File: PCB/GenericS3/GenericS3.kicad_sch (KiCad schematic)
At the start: 64 parts, among them J1 USB-C, J2 Shelly, J5 POWER, P1 33, P10 42, P11 45, P12 46, P13 47, P14 48, P15 18, P16 19, P17 14, P18 15, P19 16, P2 34, P20 17, P21 6, P22 7, P23 8, P24 9, P25 20, P26 10, P27 11, P28 12, P29 13, P3 35, P30 1, P31 2, P32 3, P33 4, P34 5, P35 21, P36 43, P37 44, P38 0, P39 ⏚, P4 36, P40 ⏚, P41 ⏚, P42 ⏚, P5 37, P6 38, P7 39, P8 40, P9 41, U2 ESP32-S3-MINI-1, U5 MD8942

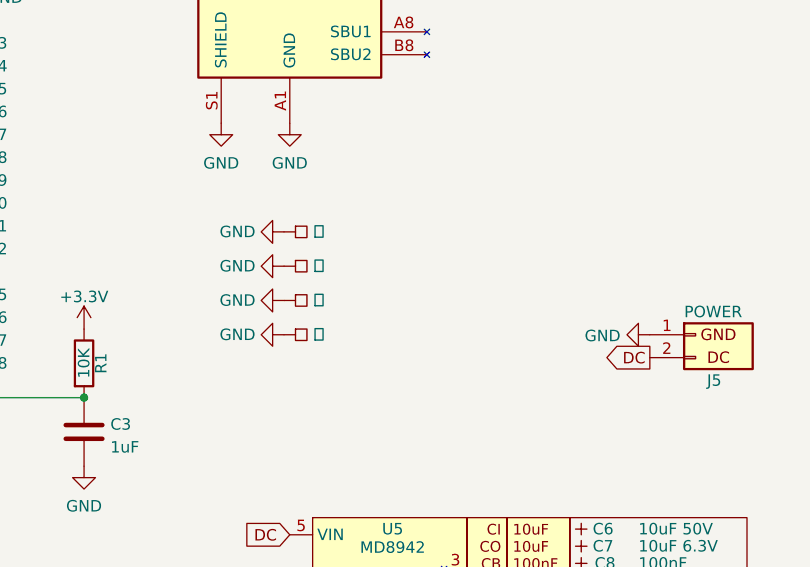
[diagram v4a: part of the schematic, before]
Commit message: Added 3V3 pads as well
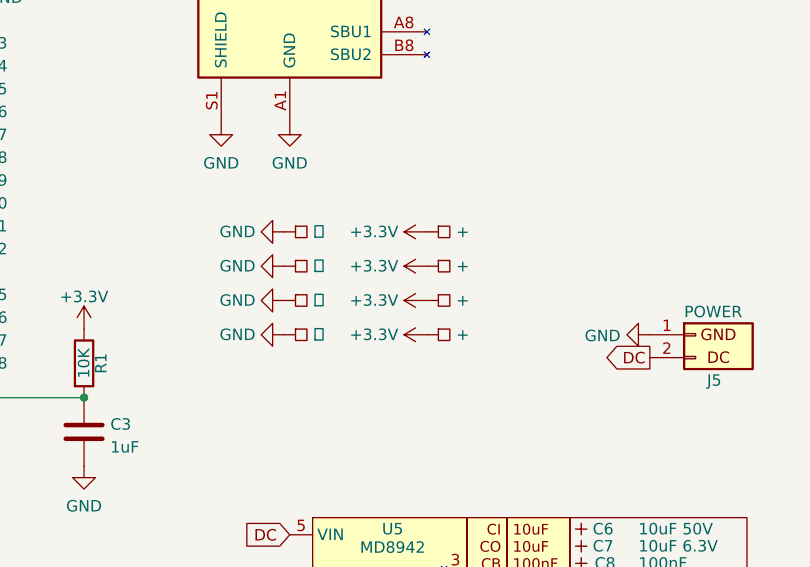
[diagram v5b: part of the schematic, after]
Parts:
- added P43, P44, P45, P46: +, RevK:Square, symbol RevK:Square
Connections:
- net +3.3V: now also P43.1 (P), P44.1 (P), P45.1 (P), P46.1 (P)
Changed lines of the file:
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@@
+    )
+  )
+  (symbol (lib_id "RevK:Square") (at 176.53 100.33 0) (unit 1)
+    (in_bom no) (on_board yes) (dnp no) (fields_autoplaced)
+    (property "Reference" "P46" (at 182.88 100.33 0)
+      (effects (font (size 1.27 1.27)) hide)
+    )
+    (property "Value" "+" (at 179.7812 100.33 0)
+      (effects (font (size 1.27 1.27)) (justify left))
+    )
+    (property "Footprint" "RevK:Square" (at 176.53 102.87 0)
+      (effects (font (size 1.27 1.27)) hide)
+    )
+    (property "Datasheet" "" (at 176.53 100.33 0)
+      (effects (font (size 1.27 1.27)) hide)
+    )
+    (pin "1")
+    (instances
+      (project "GenericS3"
+        (path "/2d210a96-f81f-42a9-8bf4-1b43c11086f3"
+          (reference "P46") (unit 1)
+        )
+      )
     )
   )
@@
     )
   )
+  (symbol (lib_id "RevK:Square") (at 176.53 96.52 0) (unit 1)
+    (in_bom no) (on_board yes) (dnp no) (fields_autoplaced)
+    (property "Reference" "P45" (at 182.88 96.52 0)
+      (effects (font (size 1.27 1.27)) hide)
+    )
+    (property "Value" "+" (at 179.7812 96.52 0)
+      (effects (font (size 1.27 1.27)) (justify left))
+    )
+    (property "Footprint" "RevK:Square" (at 176.53 99.06 0)
+      (effects (font (size 1.27 1.27)) hide)
+    )
+    (property "Datasheet" "" (at 176.53 96.52 0)
+      (effects (font (size 1.27 1.27)) hide)
+    )
+    (pin "1")
+    (instances
+      (project "GenericS3"
+        (path "/2d210a96-f81f-42a9-8bf4-1b43c11086f3"
+          (reference "P45") (unit 1)
+        )
+      )
+    )
+  )
   (symbol (lib_id "RevK:Round") (at 93.98 83.185 180) (unit 1)
     (in_bom no) (on_board yes) (dnp no)
@@
     )
   )
+  (symbol (lib_id "RevK:Square") (at 176.53 92.71 0) (unit 1)
+    (in_bom no) (on_board yes) (dnp no) (fields_autoplaced)
+    (property "Reference" "P44" (at 182.88 92.71 0)
+      (effects (font (size 1.27 1.27)) hide)
+    )
+    (property "Value" "+" (at 179.7812 92.71 0)
+      (effects (font (size 1.27 1.27)) (justify left))
+    )
+    (property "Footprint" "RevK:Square" (at 176.53 95.25 0)
+      (effects (font (size 1.27 1.27)) hide)
+    )
+    (property "Datasheet" "" (at 176.53 92.71 0)
+      (effects (font (size 1.27 1.27)) hide)
+    )
+    (pin "1")
+    (instances
+      (project "GenericS3"
+        (path "/2d210a96-f81f-42a9-8bf4-1b43c11086f3"
+          (reference "P44") (unit 1)
+        )
+      )
+    )
+  )
   (symbol (lib_id "RevK:Round") (at 93.98 57.785 180) (unit 1)
     (in_bom no) (on_board yes) (dnp no)
@@
     )
   )
+  (symbol (lib_id "RevK:Square") (at 176.53 88.9 0) (unit 1)
+    (in_bom no) (on_board yes) (dnp no) (fields_autoplaced)
+    (property "Reference" "P43" (at 182.88 88.9 0)
+      (effects (font (size 1.27 1.27)) hide)
+    )
+    (property "Value" "+" (at 179.7812 88.9 0)
+      (effects (font (size 1.27 1.27)) (justify left))
+    )
+    (property "Footprint" "RevK:Square" (at 176.53 91.44 0)
+      (effects (font (size 1.27 1.27)) hide)
+    )
+    (property "Datasheet" "" (at 176.53 88.9 0)
+      (effects (font (size 1.27 1.27)) hide)
+    )
+    (pin "1")
+    (instances
+      (project "GenericS3"
+        (path "/2d210a96-f81f-42a9-8bf4-1b43c11086f3"
+          (reference "P43") (unit 1)
+        )
+      )
+    )
+  )
+  (symbol (lib_id "power:+3.3V") (at 176.53 96.52 90) (unit 1)
+    (in_bom yes) (on_board yes) (dnp no) (fields_autoplaced)
+    (property "Reference" "#PWR020" (at 180.34 96.52 0)
+      (effects (font (size 1.27 1.27)) hide)
+    )
+    (property "Value" "+3.3V" (at 173.355 96.52 90)
+      (effects (font (size 1.27 1.27)) (justify left))
+    )
+    (property "Footprint" "" (at 176.53 96.52 0)
+      (effects (font (size 1.27 1.27)) hide)
+    )
+    (property "Datasheet" "" (at 176.53 96.52 0)
+      (effects (font (size 1.27 1.27)) hide)
+    )
+    (pin "1")
+    (instances
+      (project "GenericS3"
+        (path "/2d210a96-f81f-42a9-8bf4-1b43c11086f3"
+          (reference "#PWR020") (unit 1)
+        )
+      )
+      (project "Reference"
+        (path "/825c70b0-4860-42b7-97dc-86bfa46e06fd"
+          (reference "#PWR02") (unit 1)
+        )
+      )
+      (project "Generic"
+        (path "/babeabf2-f3b0-4ed5-8d9e-0215947e6cf3"
+          (reference "#PWR024") (unit 1)
+        )
+      )
+    )
+  )
   (symbol (lib_id "RevK:PCB") (at 250.19 172.72 0) (unit 1)
     (in_bom no) (on_board yes) (dnp no)
@@
         (path "/2d210a96-f81f-42a9-8bf4-1b43c11086f3"
           (reference "#PWR08") (unit 1)
+        )
+      )
+    )
+  )
+  (symbol (lib_id "power:+3.3V") (at 176.53 100.33 90) (unit 1)
+    (in_bom yes) (on_board yes) (dnp no) (fields_autoplaced)
+    (property "Reference" "#PWR021" (at 180.34 100.33 0)
+      (effects (font (size 1.27 1.27)) hide)
+    )
+    (property "Value" "+3.3V" (at 173.355 100.33 90)
+      (effects (font (size 1.27 1.27)) (justify left))
+    )
+    (property "Footprint" "" (at 176.53 100.33 0)
+      (effects (font (size 1.27 1.27)) hide)
+    )
+    (property "Datasheet" "" (at 176.53 100.33 0)
+      (effects (font (size 1.27 1.27)) hide)
+    )
+    (pin "1")
+    (instances
+      (project "GenericS3"
+        (path "/2d210a96-f81f-42a9-8bf4-1b43c11086f3"
+          (reference "#PWR021") (unit 1)
+        )
+      )
+      (project "Reference"
+        (path "/825c70b0-4860-42b7-97dc-86bfa46e06fd"
+          (reference "#PWR02") (unit 1)
+        )
+      )
+      (project "Generic"
+        (path "/babeabf2-f3b0-4ed5-8d9e-0215947e6cf3"
+          (reference "#PWR024") (unit 1)
         )
       )
@@
     )
   )
+  (symbol (lib_id "power:+3.3V") (at 176.53 88.9 90) (unit 1)
+    (in_bom yes) (on_board yes) (dnp no) (fields_autoplaced)
+    (property "Reference" "#PWR018" (at 180.34 88.9 0)
+      (effects (font (size 1.27 1.27)) hide)
+    )
+    (property "Value" "+3.3V" (at 173.355 88.9 90)
+      (effects (font (size 1.27 1.27)) (justify left))
+    )
+    (property "Footprint" "" (at 176.53 88.9 0)
+      (effects (font (size 1.27 1.27)) hide)
+    )
+    (property "Datasheet" "" (at 176.53 88.9 0)
+      (effects (font (size 1.27 1.27)) hide)
+    )
+    (pin "1")
+    (instances
+      (project "GenericS3"
+        (path "/2d210a96-f81f-42a9-8bf4-1b43c11086f3"
+          (reference "#PWR018") (unit 1)
+        )
+      )
+      (project "Reference"
+        (path "/825c70b0-4860-42b7-97dc-86bfa46e06fd"
+          (reference "#PWR02") (unit 1)
+        )
+      )
+      (project "Generic"
+        (path "/babeabf2-f3b0-4ed5-8d9e-0215947e6cf3"
+          (reference "#PWR024") (unit 1)
+        )
+      )
+    )
+  )
   (symbol (lib_id "Device:R") (at 138.43 103.505 0) (unit 1)
     (in_bom yes) (on_board yes) (dnp no)
@@
         )
       )
+    )
+  )
+  (symbol (lib_id "power:+3.3V") (at 176.53 92.71 90) (unit 1)
+    (in_bom yes) (on_board yes) (dnp no) (fields_autoplaced)
+    (property "Reference" "#PWR019" (at 180.34 92.71 0)
+      (effects (font (size 1.27 1.27)) hide)
+    )
+    (property "Value" "+3.3V" (at 173.355 92.71 90)
+      (effects (font (size 1.27 1.27)) (justify left))
+    )
+    (property "Footprint" "" (at 176.53 92.71 0)
+      (effects (font (size 1.27 1.27)) hide)
+    )
+    (property "Datasheet" "" (at 176.53 92.71 0)
+      (effects (font (size 1.27 1.27)) hide)
+    )
+    (pin "1")
+    (instances
+      (project "GenericS3"
+        (path "/2d210a96-f81f-42a9-8bf4-1b43c11086f3"
+          (reference "#PWR019") (unit 1)
+        )
+      )
+      (project "Reference"
+        (path "/825c70b0-4860-42b7-97dc-86bfa46e06fd"
+          (reference "#PWR02") (unit 1)
+        )
+      )
+      (project "Generic"
+        (path "/babeabf2-f3b0-4ed5-8d9e-0215947e6cf3"
+          (reference "#PWR024") (unit 1)
+        )
+      )

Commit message: Changed diode
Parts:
- D8: footprint RevK:D_1206 -> RevK:D_SMA; LCSC Part # C143805 -> C8678
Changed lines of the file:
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@@
       (effects (font (size 1.27 1.27)))
     )
-    (property "Footprint" "RevK:D_1206" (at 180.34 38.735 0)
+    (property "Footprint" "RevK:D_SMA" (at 180.34 38.735 0)
       (effects (font (size 1.27 1.27)) hide)
     )
@@
       (effects (font (size 1.27 1.27)) hide)
     )
-    (property "LCSC Part #" "C143805" (at 180.34 38.735 0)
+    (property "LCSC Part #" "C8678" (at 180.34 38.735 0)
       (effects (font (size 1.27 1.27)) hide)
     )

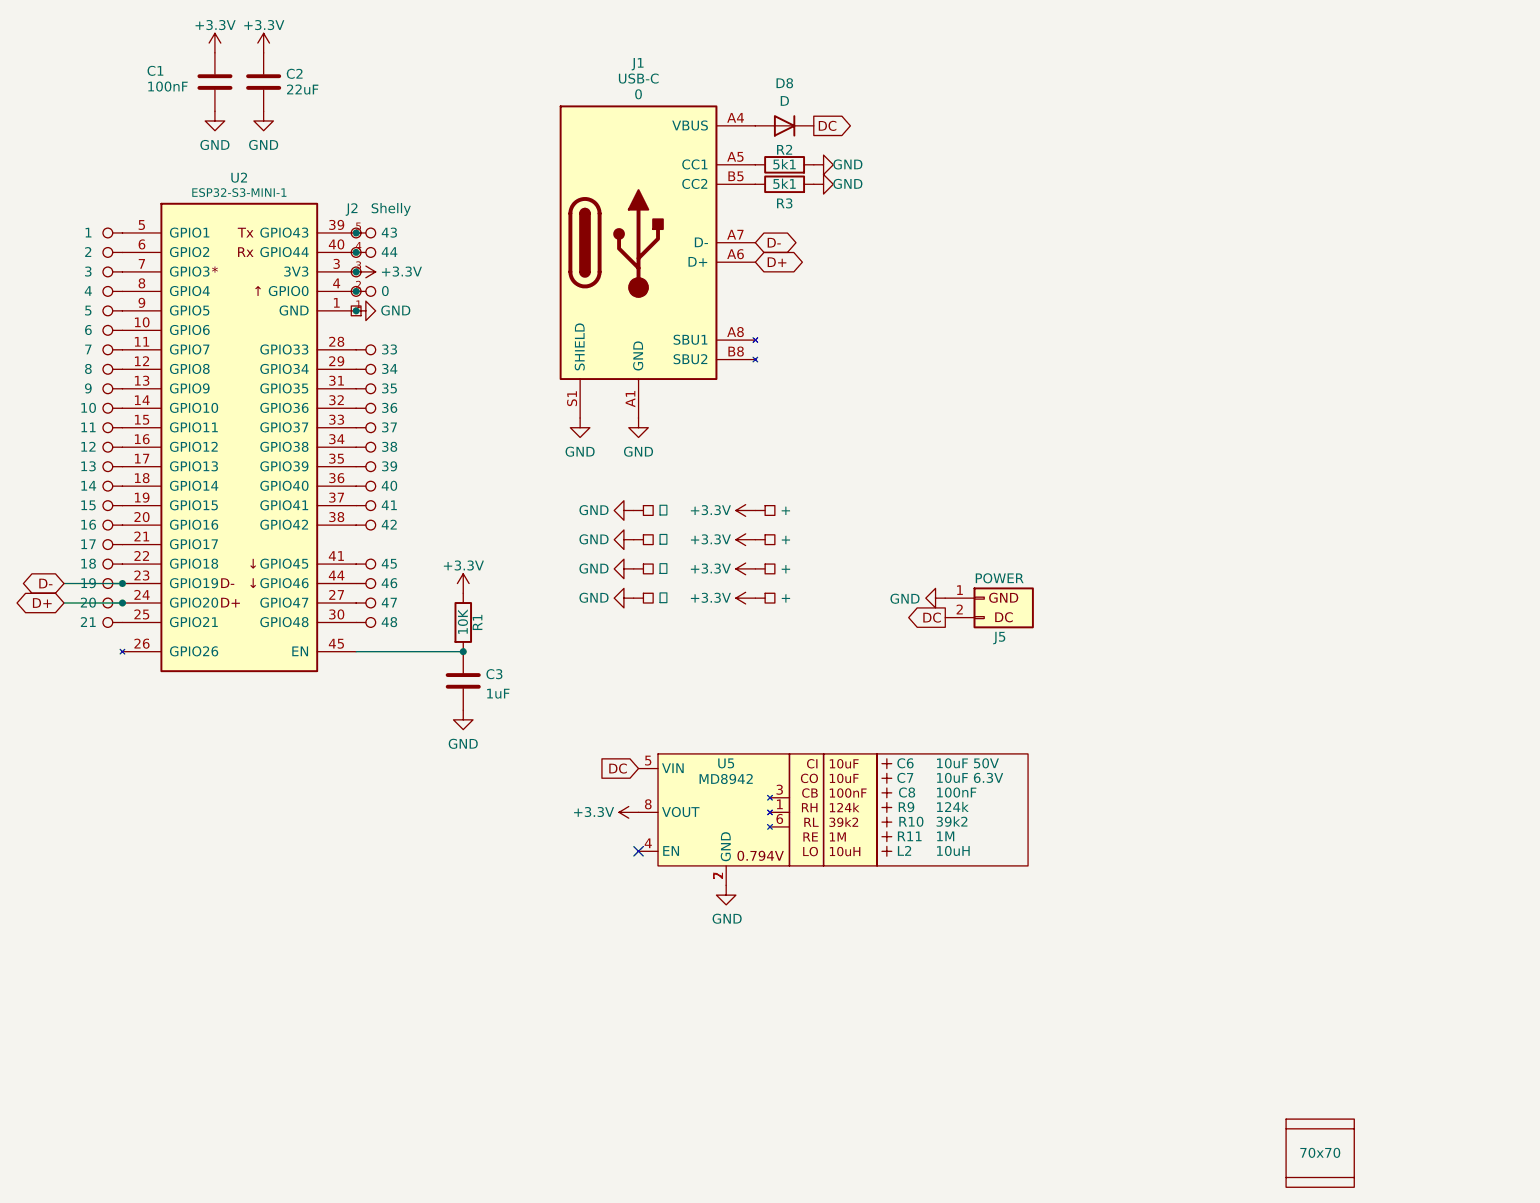
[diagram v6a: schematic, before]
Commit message: Fix diode and barcode
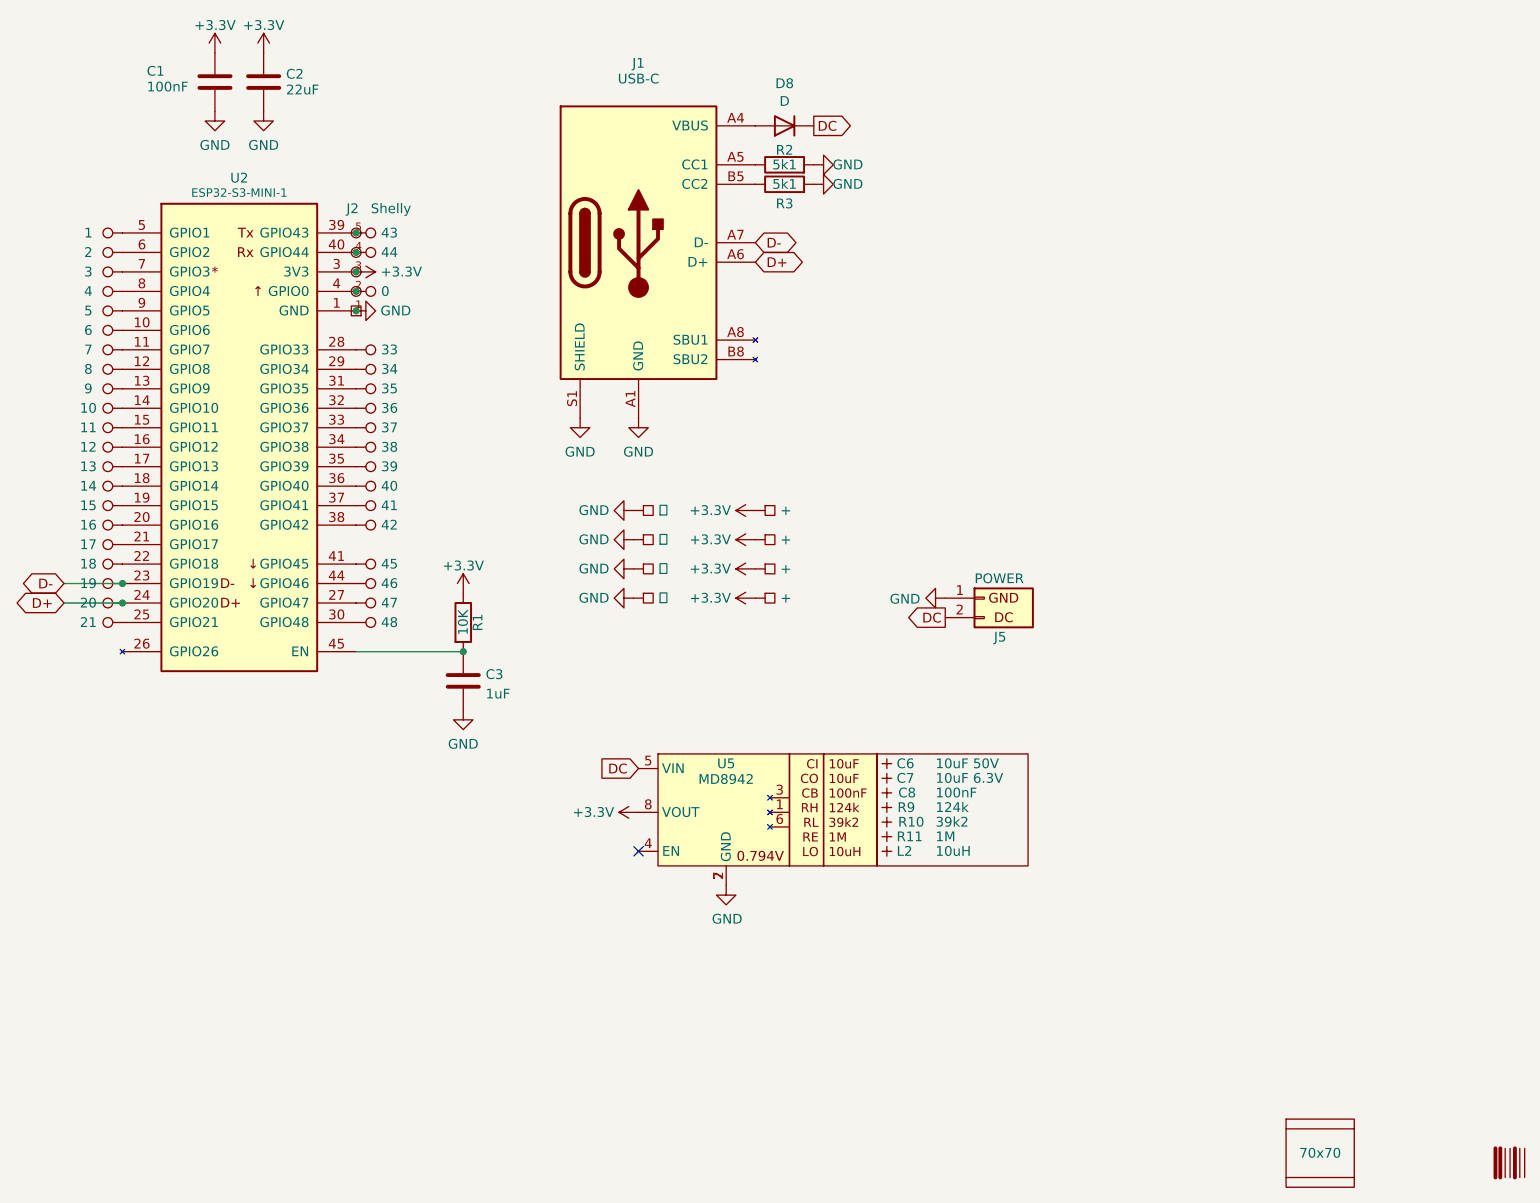
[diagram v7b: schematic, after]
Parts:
- added U1: Barcode, RevK:EAN-5060634238120, symbol RevK:Barcode
- J1: JLCPCB Rotation Offset 0 -> (none)
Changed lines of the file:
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@@
+    )
+  )
+  (symbol (lib_id "RevK:Barcode") (at 274.955 173.99 0) (unit 1)
+    (in_bom no) (on_board yes) (dnp no) (fields_autoplaced)
+    (property "Reference" "U1" (at 274.955 177.165 0)
+      (effects (font (size 1.27 1.27)) hide)
+    )
+    (property "Value" "Barcode" (at 274.955 179.07 0)
+      (effects (font (size 1.27 1.27)) hide)
+    )
+    (property "Footprint" "RevK:EAN-5060634238120" (at 274.32 174.625 0)
+      (effects (font (size 1.27 1.27)) hide)
+    )
+    (property "Datasheet" "" (at 274.32 174.625 0)
+      (effects (font (size 1.27 1.27)) hide)
+    )
+    (property "Note" "Non part, PCB printed" (at 274.955 168.275 0)
+      (effects (font (size 1.27 1.27)) hide)
+    )
+    (instances
+      (project "GenericS3"
+        (path "/2d210a96-f81f-42a9-8bf4-1b43c11086f3"
+          (reference "U1") (unit 1)
+        )
+      )
     )
   )
@@
       (effects (font (size 1.27 1.27)) hide)
     )
-    (property "JLCPCB Rotation Offset" "0" (at 161.29 34.663 0)
-      (effects (font (size 1.27 1.27)))
-    )
     (pin "A1")
